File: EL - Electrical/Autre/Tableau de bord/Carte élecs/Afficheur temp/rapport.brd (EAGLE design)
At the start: 25 parts, among them IC1 MCP23008P, IC2 MCP23008P, X1 22-23-2041

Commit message: afficheur temp
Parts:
- moved R1 13.7 mm to (21.9, 22.2), turned to 180 degrees
- moved C3 6.35 mm to (3.81, 22.9)
- moved C2 4.77 mm to (-1.27, 22.9)
- moved X1 1.59 mm to (-1.27, 29.8)
- moved R2 1.59 mm to (-1.27, 15.6)
- turned IC2 to 0 degrees
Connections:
- net GP10: no longer R1A.2
- net GP11: no longer R1B.2
- net GP13: no longer R1F.2, R2D.2
- net GP15: no longer R2A.2
- net GP16: now also R2D.2
- net GP17: now also R2E.2
- net GP20: now also R3AB.2; no longer R2B.2
- net GP21: now also R2F.2
- net GP22: now also R2G.2
- net GP23: now also R2A.2; no longer R2E.2
- net GP24: now also R2B.2; no longer R2F.2
- net GP25: now also R1F.2; no longer R2G.2
- net GP26: now also R1A.2
- net GP27: now also R1B.2; no longer R3AB.2
- net SCL: now also C2.1, R1.1, X1.3; no longer C3.1, R2.2, X1.2
- net SDA: now also C3.1, R2.2, X1.2; no longer C2.1, R1.1, X1.3
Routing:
- net +5V: track 0.00 -> 128.7 mm
- net GND: track 0.00 -> 62.6 mm
- net SDA: track 0.00 -> 51.5 mm
- net SCL: track 0.00 -> 43.3 mm
- net GP20: track 0.00 -> 39.5 mm
- net GP24: track 0.00 -> 36.9 mm
- net GP23: track 0.00 -> 36.9 mm
- net GP22: track 0.00 -> 36.9 mm
- net GP21: track 0.00 -> 36.9 mm
- net GP11: track 0.00 -> 36.6 mm
- net GP10: track 0.00 -> 36.6 mm
- net GP27: track 0.00 -> 31.7 mm
- net GP26: track 0.00 -> 31.7 mm
- net GP25: track 0.00 -> 31.7 mm
- net GP17: track 7.63 -> 36.6 mm
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
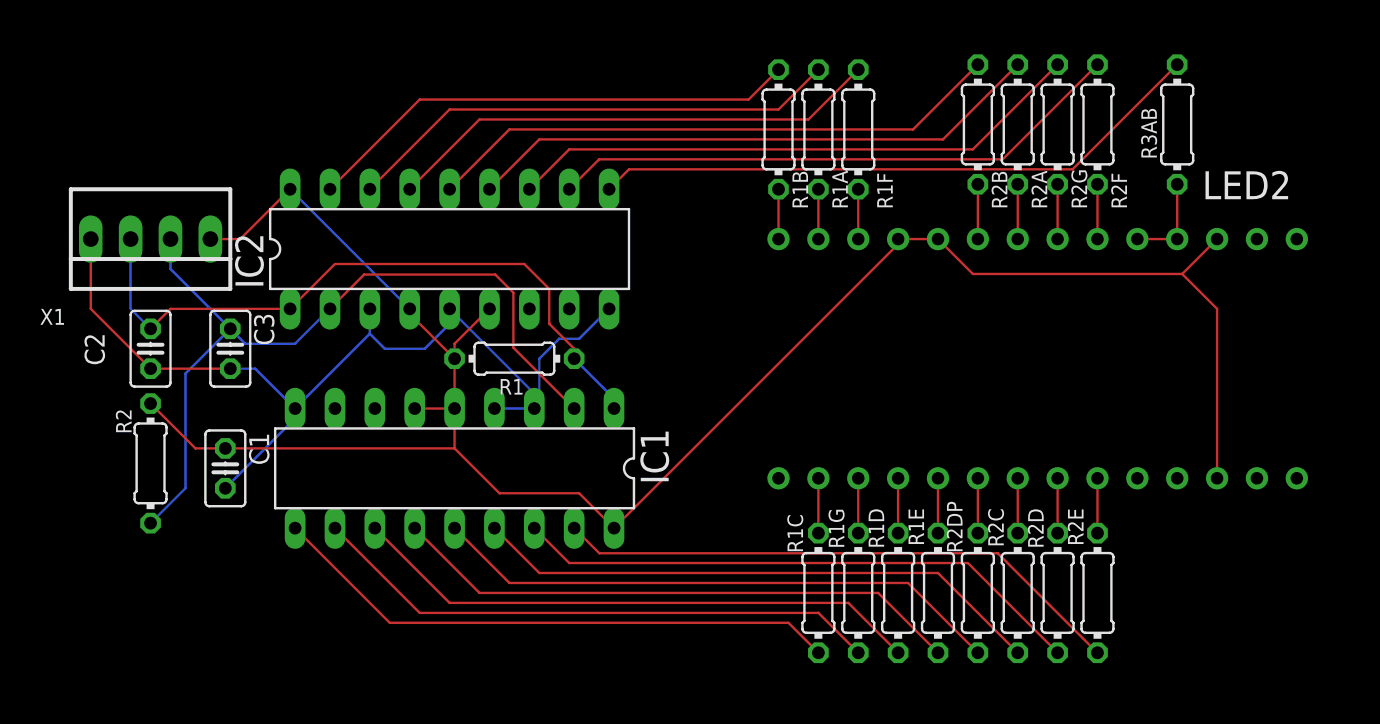
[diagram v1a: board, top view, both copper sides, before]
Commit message: Afficheur 3 digit + plan carte tdb
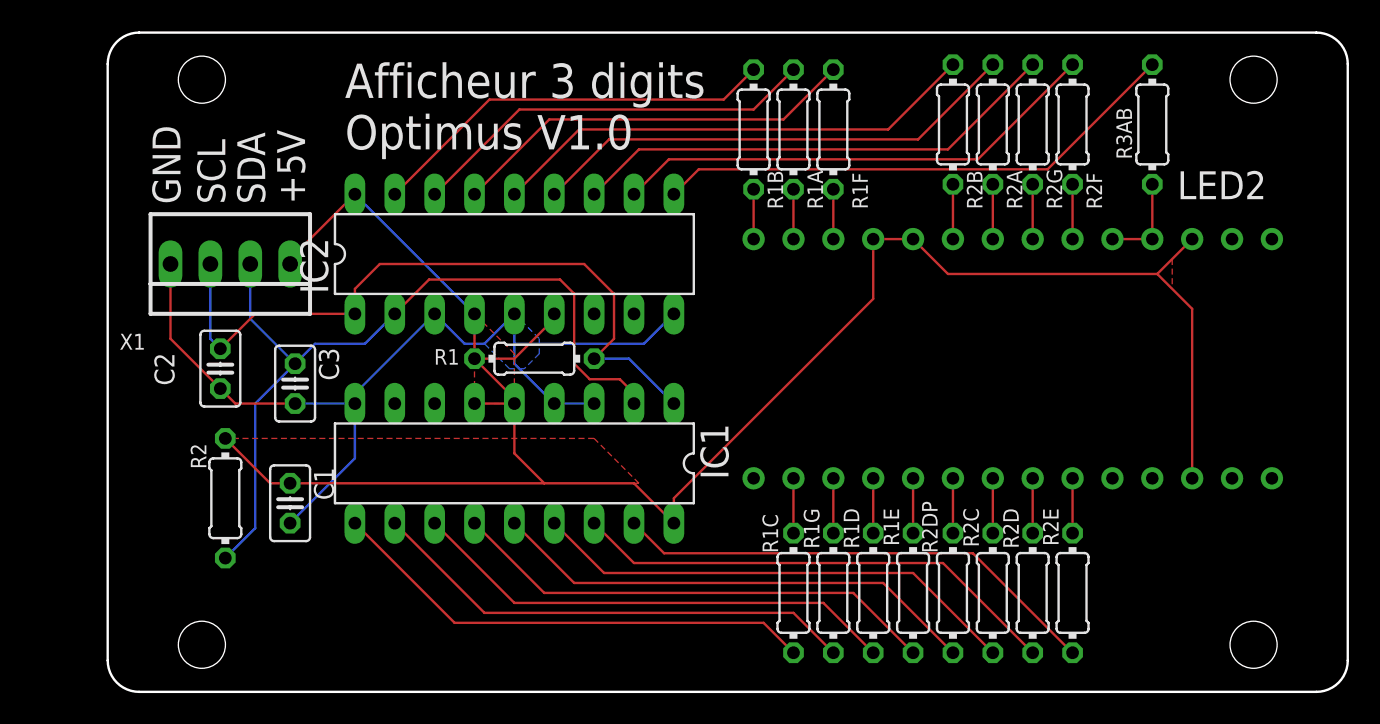
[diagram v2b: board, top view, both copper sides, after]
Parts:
- moved X1 5.32 mm to (3.81, 28.3)
- moved R2 5.26 mm to (3.49, 13.3)
- moved C1 4.69 mm to (7.62, 13.0)
- moved C3 4.69 mm to (7.94, 20.6)
- moved C2 4.62 mm to (3.17, 21.6)
- moved IC2 4.14 mm to (21.9, 28.9)
- moved IC1 3.82 mm to (21.9, 15.6)
- moved R1E 1.59 mm to (47.3, 7.30)
- moved R2B 1.59 mm to (49.8, 37.1)
- moved R2DP 1.59 mm to (49.8, 7.30)
- moved R3AB 1.59 mm to (62.5, 37.1)
- moved LED2 1.59 mm to (53.7, 22.2)
- moved R1A 1.59 mm to (39.7, 36.8)
- moved R1B 1.59 mm to (37.1, 36.8)
- moved R1C 1.59 mm to (39.7, 7.30)
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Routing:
- net GP20: track 39.5 -> 33.9 mm
- net GP26: track 31.7 -> 26.1 mm
- net GP24: track 36.9 -> 31.4 mm
- net GP27: track 31.7 -> 26.1 mm
- net GP25: track 31.7 -> 26.1 mm
- net GP23: track 36.9 -> 31.4 mm
- net GP22: track 36.9 -> 31.4 mm
- net GP21: track 36.9 -> 31.4 mm
- net GP15: track 36.6 -> 31.4 mm
- net GP14: track 36.6 -> 31.4 mm
- net GP13: track 36.6 -> 31.4 mm
- net GP11: track 36.6 -> 31.4 mm
- net GP10: track 36.6 -> 31.4 mm
- net GP17: track 36.6 -> 31.4 mm
- net GP16: track 36.6 -> 31.4 mm
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- added copper zone on layer 1, net +5V
- added copper zone on layer 16, net GND
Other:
- board outline added: 79 x 42 mm
- board text added: "+5V"
- board text added: "Afficheur 3 digits Optimus V1.0"
- board text added: "GND"
- board text added: "SCL"
- board text added: "SDA"
